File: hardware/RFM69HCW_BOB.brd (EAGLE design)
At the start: 27.9 x 20.3 mm, 13 parts, among them U1 RFM69HCW

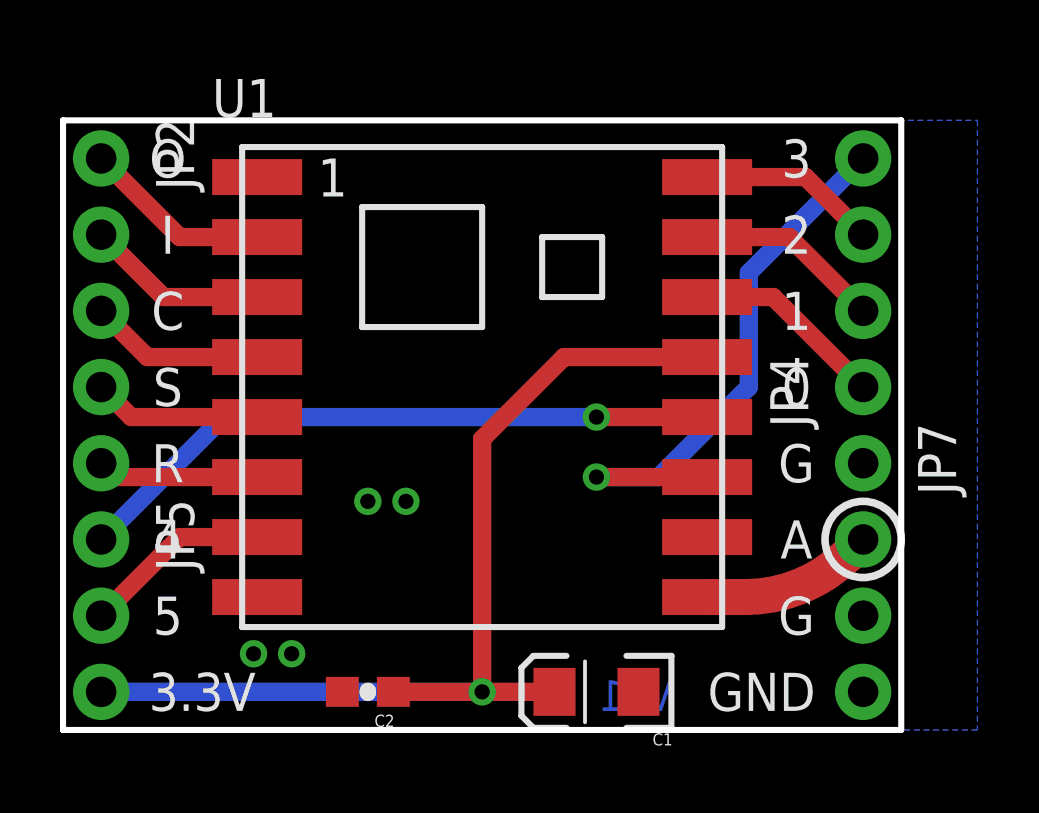
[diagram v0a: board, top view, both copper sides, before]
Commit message: Minor silk updates
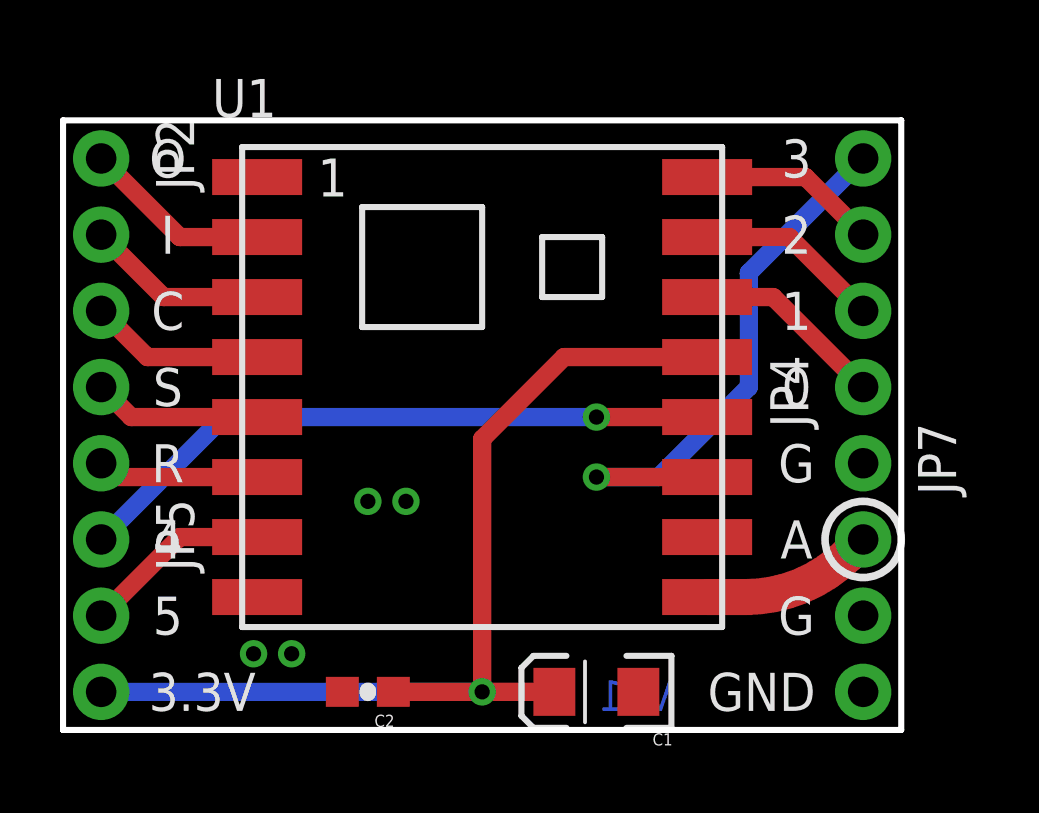
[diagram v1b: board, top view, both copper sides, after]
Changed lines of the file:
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@@
 <grid distance="0.05" unitdist="inch" unit="inch" style="lines" multiple="2" display="yes" altdistance="0.0125" altunitdist="inch" altunit="inch"/>
 <layers>
-<layer number="1" name="Top" color="4" fill="1" visible="no" active="yes"/>
+<layer number="1" name="Top" color="4" fill="1" visible="yes" active="yes"/>
 <layer number="2" name="Route2" color="1" fill="3" visible="no" active="no"/>
 <layer number="3" name="Route3" color="4" fill="3" visible="no" active="no"/>
@@
 <layer number="14" name="Route14" color="1" fill="6" visible="no" active="no"/>
 <layer number="15" name="Route15" color="4" fill="6" visible="no" active="no"/>
-<layer number="16" name="Bottom" color="1" fill="1" visible="no" active="yes"/>
+<layer number="16" name="Bottom" color="1" fill="1" visible="yes" active="yes"/>
 <layer number="17" name="Pads" color="2" fill="1" visible="yes" active="yes"/>
 <layer number="18" name="Vias" color="2" fill="1" visible="yes" active="yes"/>
 <layer number="19" name="Unrouted" color="6" fill="1" visible="yes" active="yes"/>
 <layer number="20" name="Dimension" color="15" fill="1" visible="yes" active="yes"/>
-<layer number="21" name="tPlace" color="7" fill="1" visible="no" active="yes"/>
-<layer number="22" name="bPlace" color="7" fill="1" visible="yes" active="yes"/>
+<layer number="21" name="tPlace" color="7" fill="1" visible="yes" active="yes"/>
+<layer number="22" name="bPlace" color="7" fill="1" visible="no" active="yes"/>
 <layer number="23" name="tOrigins" color="15" fill="1" visible="no" active="yes"/>
-<layer number="24" name="bOrigins" color="15" fill="1" visible="yes" active="yes"/>
+<layer number="24" name="bOrigins" color="15" fill="1" visible="no" active="yes"/>
 <layer number="25" name="tNames" color="7" fill="1" visible="no" active="yes"/>
 <layer number="26" name="bNames" color="7" fill="1" visible="no" active="yes"/>
@@
 <polygon width="0.2032" layer="16" isolate="0.3048">
 <vertex x="0" y="20.32"/>
-<vertex x="30.48" y="20.32"/>
-<vertex x="30.48" y="0"/>
+<vertex x="27.94" y="20.32"/>
+<vertex x="27.94" y="0"/>
 <vertex x="0" y="0"/>
 </polygon>
